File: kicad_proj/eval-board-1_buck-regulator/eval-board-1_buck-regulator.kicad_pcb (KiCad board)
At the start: 2 copper layers, 0 parts

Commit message: Updates from livestream
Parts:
- added C1: GRM32ER71C226KEA8, eval-board-1_buck-regulator:CAPACITOR_1210N, F.Cu at (7.50, 5.00)
- added C10: 4.7u, eval-board-1_buck-regulator:CAPACITOR_0603N, F.Cu at (23.7, 22.8)
- added C11: GRM32ER71E226ME15K, eval-board-1_buck-regulator:CAPACITOR_1210N, F.Cu at (33.9, 17.5)
- added C12: 1u, eval-board-1_buck-regulator:CAPACITOR_0402N, F.Cu at (21.0, 23.2)
- added C13: GRM32ER71E226ME15K, eval-board-1_buck-regulator:CAPACITOR_1210N, F.Cu at (30.4, 17.5)
- added C14: GRM188R61H225ME11D, eval-board-1_buck-regulator:CAPACITOR_0603N, F.Cu at (27.9, 16.8)
- added C15: 0.1uF, eval-board-1_buck-regulator:CAPACITOR_0402N, F.Cu at (21.6, 13.8)
- added C16: GRM32ER71C226KEA8, eval-board-1_buck-regulator:CAPACITOR_1210N, F.Cu at (43.8, 25.6)
- added C17: GRM32ER71C226KEA8, eval-board-1_buck-regulator:CAPACITOR_1210N, F.Cu at (43.8, 30.3)
- added C18: GRM32ER71C226KEA8, eval-board-1_buck-regulator:CAPACITOR_1210N, F.Cu at (47.1, 25.6)
- added C2: UCH1V470MCS1GS, eval-board-1_buck-regulator:CAPAE660X580L260X65N, F.Cu at (20.5, 5.00)
- added C3: UCH1V470MCS1GS, eval-board-1_buck-regulator:CAPAE660X580L260X65N, F.Cu at (28.0, 5.00)
- added C4: GRM32ER71C226KEA8, eval-board-1_buck-regulator:CAPACITOR_1210N, F.Cu at (15.0, 5.00)
- added C5: GRM32ER71E226ME15K, eval-board-1_buck-regulator:CAPACITOR_1210N, F.Cu at (30.4, 12.5)
- added C6: GRM32ER71E226ME15K, eval-board-1_buck-regulator:CAPACITOR_1210N, F.Cu at (33.9, 12.5)
- added C7: GRM188R61H225ME11D, footprints:CAPACITOR_0603N, F.Cu at (22.2, 22.8)
- added C8: GRM32ER71E226ME15K, eval-board-1_buck-regulator:CAPACITOR_1210N, F.Cu at (37.4, 12.5)
- added C9: GRM32ER71E226ME15K, eval-board-1_buck-regulator:CAPACITOR_1210N, F.Cu at (37.4, 17.5)
- added D1: LED, eval-board-1_buck-regulator:CAPACITOR_0603N, F.Cu at (10.0, 3.50)
- added D2: LED, eval-board-1_buck-regulator:CAPACITOR_0603N, F.Cu at (49.8, 24.2)
- added FB1: 74279221100, eval-board-1_buck-regulator:CAPACITOR_1206N, F.Cu at (12.0, 5.00)
- added J1: Conn_01x02, Connector_PinHeader_2.54mm:PinHeader_1x02_P2.54mm_Vertical, F.Cu at (3.17, 3.65)
- added J2: Conn_01x06, Connector_PinHeader_2.54mm:PinHeader_1x06_P2.54mm_Vertical, F.Cu at (3.20, 10.5)
- added J3: Conn_01x02, Connector_PinHeader_2.54mm:PinHeader_1x02_P2.54mm_Vertical, F.Cu at (53.1, 24.3)
- added JP1: Jumper_NC_Dual, Connector_PinHeader_2.54mm:PinHeader_1x03_P2.54mm_Vertical, F.Cu at (12.2, 10.5)
- added JP2: Jumper, Connector_PinHeader_2.54mm:PinHeader_1x02_P2.54mm_Vertical, F.Cu at (17.7, 28.4)
- added L1: PA4343.102NLT, eval-board-1_buck-regulator:PA4343_PM4343, F.Cu at (34.6, 27.1)
- added R1: 220, eval-board-1_buck-regulator:CAPACITOR_0402N, F.Cu at (6.60, 23.2)
- added R10: 10K, eval-board-1_buck-regulator:CAPACITOR_0402N, F.Cu at (10.9, 15.0)
- added R11: 8.87K, eval-board-1_buck-regulator:CAPACITOR_0402N, F.Cu at (16.9, 19.3)
- added R12: 10K, eval-board-1_buck-regulator:CAPACITOR_0402N, F.Cu at (17.6, 16.9)
- added R13: 10K, eval-board-1_buck-regulator:CAPACITOR_0402N, F.Cu at (17.6, 15.9)
- added R14: 2.2, eval-board-1_buck-regulator:CAPACITOR_0402N, F.Cu at (22.7, 13.8)
- added R15: 220, eval-board-1_buck-regulator:CAPACITOR_0402N, F.Cu at (49.8, 26.6)
- added R2: 220, eval-board-1_buck-regulator:CAPACITOR_0402N, F.Cu at (6.60, 18.1)
- added R3: 10K, eval-board-1_buck-regulator:CAPACITOR_0402N, F.Cu at (10.9, 16.0)
- added R4: 220, eval-board-1_buck-regulator:CAPACITOR_0402N, F.Cu at (6.60, 20.6)
- added R5: 10K, eval-board-1_buck-regulator:CAPACITOR_0402N, F.Cu at (10.9, 17.0)
- added R6: 510, eval-board-1_buck-regulator:CAPACITOR_0402N, F.Cu at (10.0, 6.50)
- added R7: 10K, eval-board-1_buck-regulator:CAPACITOR_0402N, F.Cu at (20.7, 25.3)
- added R8: 8.87K, eval-board-1_buck-regulator:CAPACITOR_0402N, F.Cu at (16.9, 18.3)
- added R9: 8.87K, eval-board-1_buck-regulator:CAPACITOR_0402N, F.Cu at (17.7, 20.3)
- added TP1: TestPoint, TestPoint:TestPoint_Pad_1.5x1.5mm, F.Cu at (22.2, 11.2)
- added TP2: TestPoint, TestPoint:TestPoint_Pad_1.5x1.5mm, F.Cu at (23.8, 28.4)
- added U1: SIC453ED-T1-GE3, eval-board-1_buck-regulator:SiC45X, F.Cu at (22.9, 18.0)
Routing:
- net GND: track 0.00 -> 101.5 mm, vias 0 -> 21
- net +5V: track 0.00 -> 66.2 mm
- net Net-(C11-Pad1): track 0.00 -> 63.6 mm, vias 0 -> 2
- net /SCL: track 0.00 -> 26.7 mm, vias 0 -> 2
- net /VDD: track 0.00 -> 22.6 mm, vias 0 -> 2
- net /SDA: track 0.00 -> 21.6 mm, vias 0 -> 2
- net /PGOOD: track 0.00 -> 20.6 mm, vias 0 -> 2
- net /SALERT: track 0.00 -> 14.0 mm, vias 0 -> 2
- net Net-(TP2-Pad1): track 0.00 -> 11.0 mm
- net +12V: track 0.00 -> 10.3 mm
- net Net-(L1-Pad1): track 0.00 -> 9.91 mm
- net /EXTERN_VTG: track 0.00 -> 8.48 mm
- net /EN: track 0.00 -> 8.35 mm
- net /PULLUP_VTG: track 0.00 -> 6.80 mm
- net Net-(TP1-Pad1): track 0.00 -> 4.36 mm, vias 0 -> 2
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- added copper zone on In1.Cu, net GND
- added copper zone on In2.Cu, net GND
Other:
- board outline added: 107 x 43 mm
- copper layers 2 -> 4

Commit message: Livestream updates
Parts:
- added C19: UCH1V470MCS1GS, eval-board-1_buck-regulator:CAPAE660X580L260X65N, F.Cu at (42.7, 18.5)
- added H1: MountingHole_Pad, MountingHole:MountingHole_2.7mm_M2.5_Pad_Via, F.Cu at (51.0, 6.05)
- added H2: MountingHole_Pad, MountingHole:MountingHole_2.7mm_M2.5_Pad_Via, F.Cu at (13.5, 12.8)
- added H3: MountingHole_Pad, MountingHole:MountingHole_2.7mm_M2.5_Pad_Via, F.Cu at (15.5, 32.2)
- C4: value GRM32ER71C226KEA8 -> UCH1V470MCS1GS; footprint eval-board-1_buck-regulator:CAPACITOR_1210N -> eval-board-1_buck-regulator:CAPAE660X580L260X65N
- J1, J3: footprint Connector_PinHeader_2.54mm:PinHeader_1x02_P2.54mm_Vertical -> eval-board-1_buck-regulator:1935776
- moved C4 26.0 mm to (41.0, 5.90)
- moved JP1 23.0 mm to (10.1, 33.4)
- moved D1 15.1 mm to (1.25, 15.8), turned to 90 degrees
- moved R2 11.0 mm to (9.70, 26.9), turned to 90 degrees
- moved R6 10.8 mm to (1.25, 12.8), turned to -90 degrees
- moved C18 7.72 mm to (42.8, 32.0), turned to -90 degrees
- moved R5 7.50 mm to (9.70, 24.4), turned to 90 degrees
- moved C16 6.74 mm to (46.0, 32.0), turned to -90 degrees
- moved TP2 6.33 mm to (17.5, 27.8), turned to 90 degrees
- moved JP2 6.29 mm to (12.3, 25.1), turned to 0 degrees
- moved J2 6.03 mm to (5.02, 16.2)
- moved R1 6.02 mm to (8.22, 23.9)
- moved R4 6.02 mm to (8.22, 26.4)
- moved J3 5.94 mm to (51.8, 18.5), turned to -90 degrees
- moved C1 5.50 mm to (13.0, 5.00)
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- renumbered R2 to R1, R3 to R2, R1 to R3
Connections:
- J2 pad 3: /EXTERN_VTG -> Net-(J2-Pad3)
- J2 pad 6: Net-(J2-Pad6) -> /EXTERN_VTG
- R3 pad 1: Net-(J2-Pad6) -> Net-(J2-Pad3)
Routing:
- net /PULLUP_VTG: track 6.80 -> 37.9 mm
- net Net-(C11-Pad1): track 63.6 -> 47.5 mm
- net /SCL: track 26.7 -> 11.0 mm, vias 2 -> 0
- net +5V: track 66.2 -> 79.4 mm
- net /SDA: track 21.6 -> 8.67 mm, vias 2 -> 0
- net /PGOOD: track 20.6 -> 10.7 mm, vias 2 -> 0
- net /SALERT: track 14.0 -> 7.78 mm, vias 2 -> 0
- net /VDD: track 22.6 -> 17.1 mm, vias 2 -> 0
- net /EXTERN_VTG: track 8.48 -> 4.52 mm
- net Net-(J2-Pad6): track 2.90 -> 0.00 mm
- net Net-(J2-Pad3): track 0.00 -> 2.53 mm
- net GND: track 101.5 -> 103.2 mm, vias 21 -> 14
- net +12V: track 10.3 -> 8.90 mm
- net Net-(D2-Pad2): track 1.15 -> 1.68 mm
- added copper zone on B.Cu, net +12V
- added copper zone on F.Cu, net +12V
- added copper zone on F.Cu, net +5V
- added copper zone on B.Cu, net Net-(C11-Pad1)
- added copper zone on F.Cu, net Net-(C11-Pad1)
- added copper zone on F.Cu, net Net-(L1-Pad1)
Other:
- board size 107 x 43 mm -> 57.2 x 37 mm

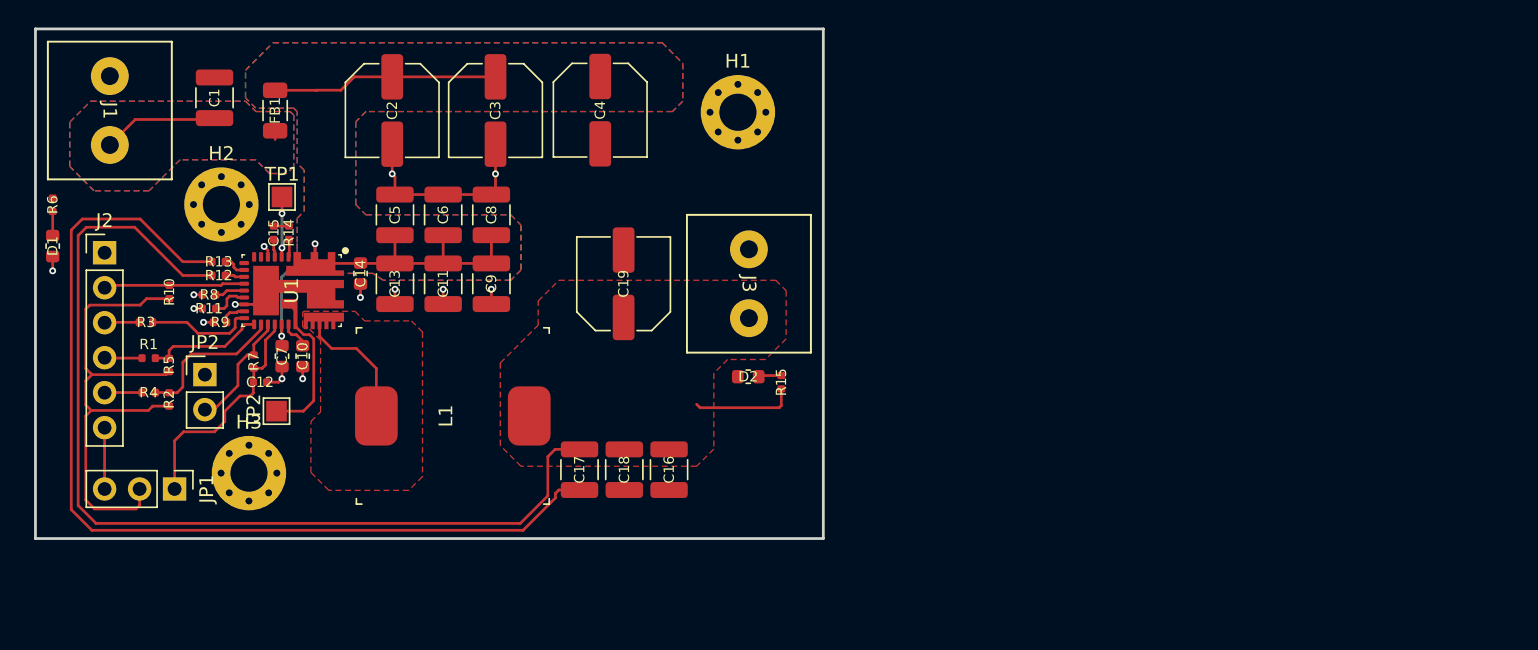
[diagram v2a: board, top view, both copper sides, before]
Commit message: Updates silkscreen to board
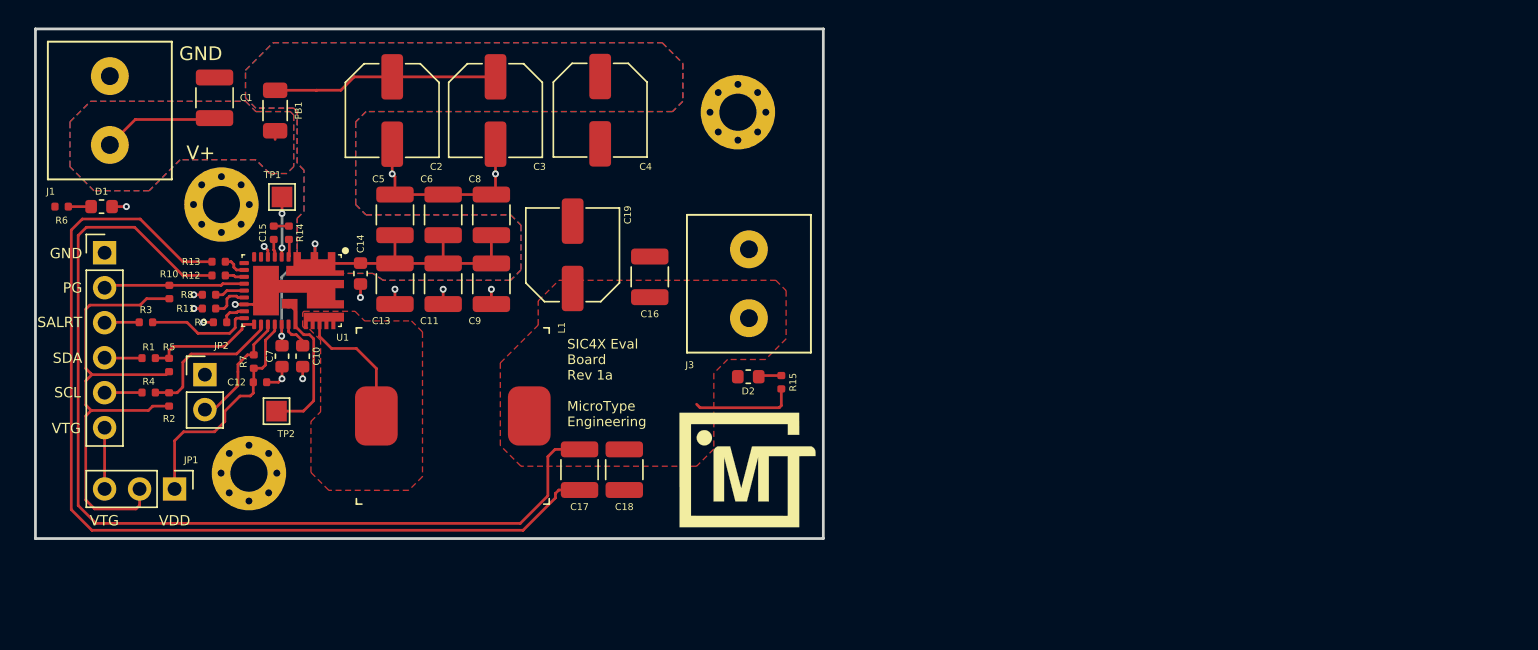
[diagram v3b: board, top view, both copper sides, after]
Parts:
- added G***: LOGO, footprints:MTE_LOGO_25.4MM, F.Cu at (51.7, 32.0)
- moved C16 14.1 mm to (44.6, 18.0), turned to 90 degrees
- moved D1 4.56 mm to (4.80, 12.9), turned to 180 degrees
- moved C19 4.25 mm to (39.0, 16.4)
- moved R6 0.66 mm to (1.90, 12.9), turned to 0 degrees
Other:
- board text added: "GND"
- board text added: "PG"
- board text added: "SALRT"
- board text added: "SCL"
- board text added: "SDA"
- board text added: "SIC4X Eval Board Rev 1a MicroType Engineering"
- board text added: "V+"
- board text added: "VDD"
- board text added: "VTG"

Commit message: Add fill keepout for analog lines, 12v led trace, slight adjust to fills
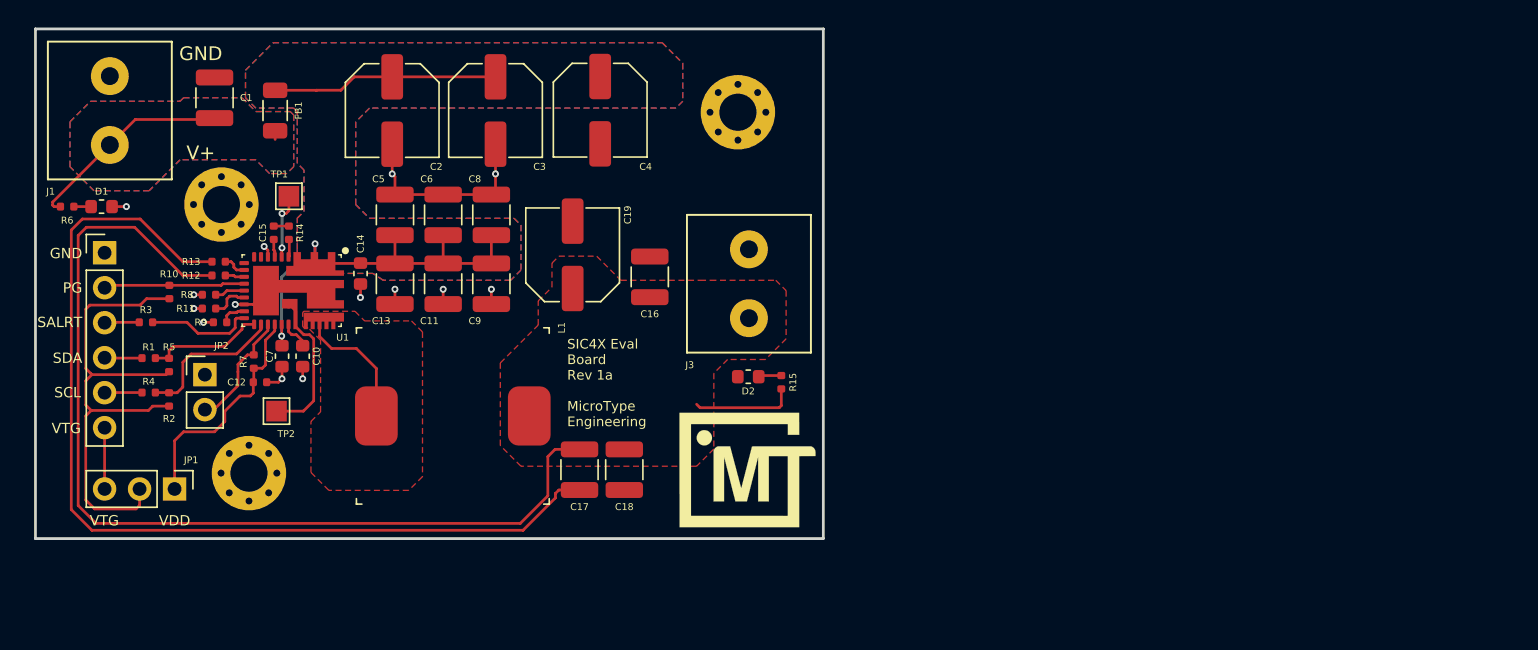
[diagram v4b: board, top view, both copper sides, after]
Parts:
- moved TP1 0.50 mm to (18.4, 12.2)
- moved R6 0.40 mm to (2.30, 12.9)
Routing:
- net +12V: track 8.90 -> 15.6 mm
- net Net-(TP1-Pad1): track 4.36 -> 4.94 mm
- added copper zone on F.Cu, net GND

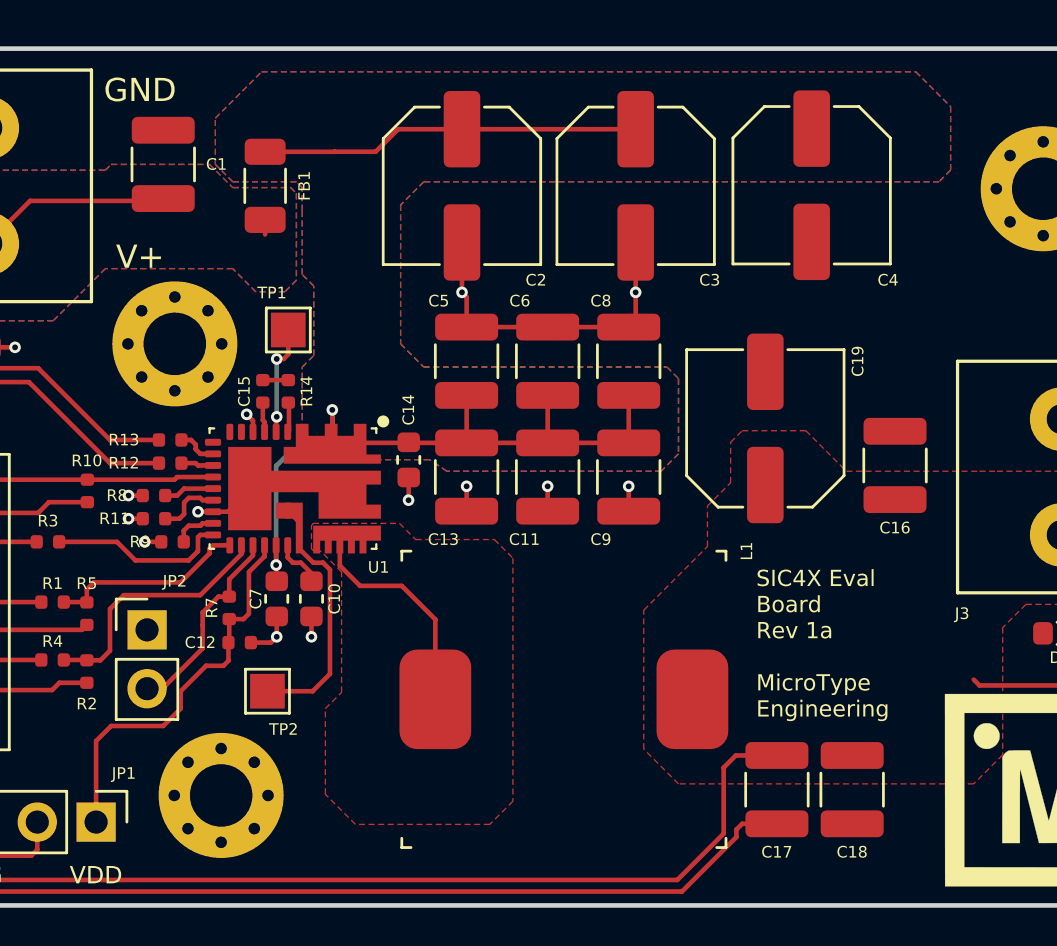
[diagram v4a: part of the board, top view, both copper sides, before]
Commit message: Added vias around caps
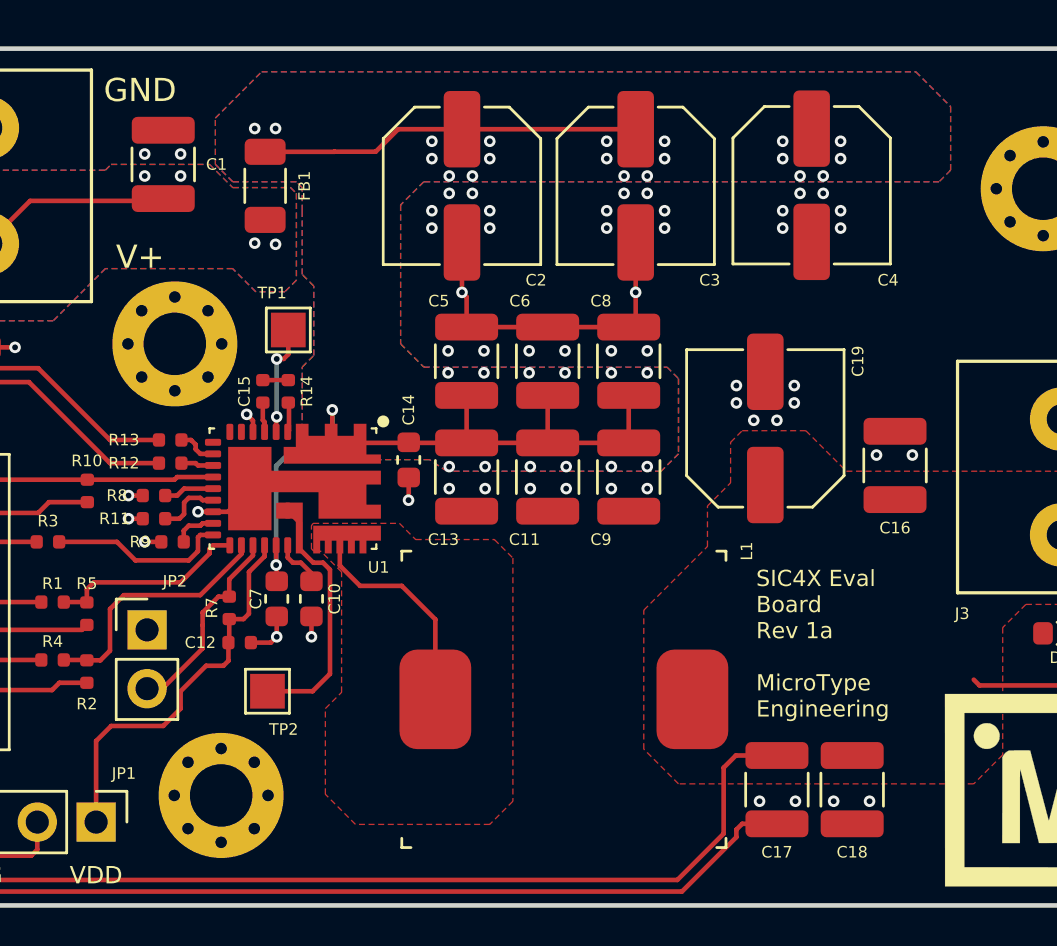
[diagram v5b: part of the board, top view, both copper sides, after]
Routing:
- net GND: track 103.2 -> 99.9 mm, vias 14 -> 55
- net +12V: track 15.6 -> 15.0 mm, vias 0 -> 4
- net Net-(C11-Pad1): vias 2 -> 34

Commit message: Added general stitching vias
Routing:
- net Net-(C11-Pad1): vias 34 -> 48
- net GND: vias 55 -> 100
- net +12V: vias 4 -> 7
